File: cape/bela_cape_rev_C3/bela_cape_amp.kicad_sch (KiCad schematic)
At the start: 14 parts, among them IC1 PAM8406

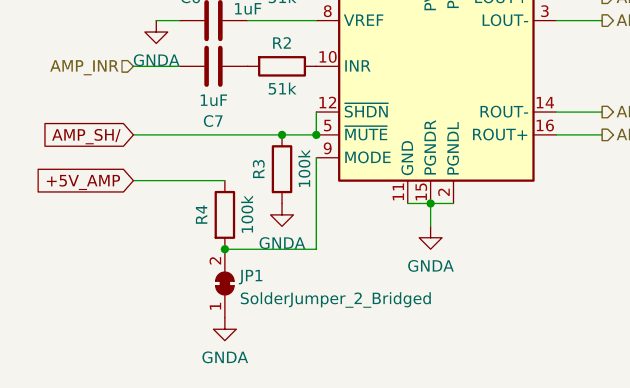
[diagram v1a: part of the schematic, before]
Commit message: removed sym-lib-table with a reference to an unused and obsolete local library
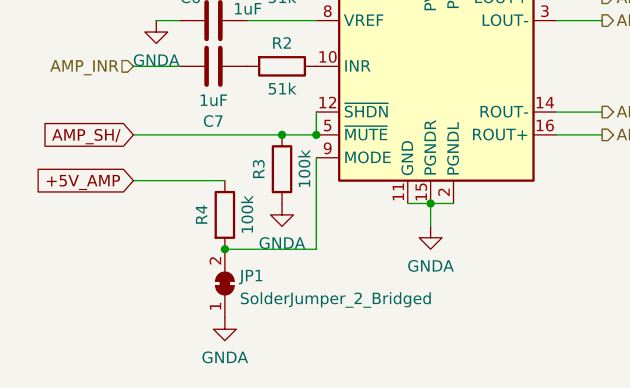
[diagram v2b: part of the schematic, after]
